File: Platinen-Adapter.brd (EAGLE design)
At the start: 26 x 100 mm, 2 parts, among them X1 MAC64L

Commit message: Layouts angepasst
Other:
- board text added: "1"
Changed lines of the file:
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@@
 <dimension x1="0" y1="-0.47" x2="0" y2="99.53" x3="-16.51" y3="49.53" textsize="1.778" layer="47"/>
 <dimension x1="0" y1="-0.47" x2="26" y2="-0.47" x3="13" y3="-12.7" textsize="1.778" layer="47"/>
-<text x="19.05" y="64.77" size="1.778" layer="25" rot="R90" align="top-center">Rev 2019/04
+<text x="18.415" y="69.85" size="2.54" layer="25" font="vector" ratio="15" rot="R90" align="top-center">Rev 2019/04
 (c) Peter Müller</text>
-<text x="19.05" y="34.29" size="1.778" layer="25" rot="R90" align="top-center">HomePi
+<text x="18.415" y="30.48" size="2.54" layer="25" font="vector" ratio="15" rot="R90" align="top-center">HomePi
 Adapter-Board</text>
+<text x="18.415" y="10.795" size="1.778" layer="25" font="vector" ratio="10" align="center">1</text>
+<text x="18.415" y="69.85" size="2.54" layer="26" font="vector" ratio="15" rot="SMR270" align="top-center">HomePi
+Adapter-Board</text>
+<text x="18.415" y="30.48" size="2.54" layer="26" font="vector" ratio="15" rot="SMR270" align="top-center">Rev 2019/04
+(c) Peter Müller</text>
 </plain>
 <attributes>
@@
 <classes>
 <class number="0" name="default" width="0" drill="0">
+</class>
+<class number="1" name="24V" width="0.8128" drill="0">
+<clearance class="1" value="0.4064"/>
 </class>
 </classes>
@@
 <elements>
 <element name="SV1" library="64-pol-verbinder" package="1X31" value="" x="15.875" y="48.26" smashed="yes" rot="R90">
-<attribute name="NAME" x="14.5288" y="91.3638" size="1.27" layer="25" ratio="10"/>
 <attribute name="VALUE" x="19.05" y="10.16" size="1.27" layer="27" rot="R90"/>
 </element>
@@
 <wire x1="5.08" y1="83.82" x2="10.16" y2="83.82" width="0.8128" layer="1"/>
 </signal>
-<signal name="+24V">
+<signal name="+24V" class="1">
 <contactref element="X1" pad="A32"/>
 <contactref element="X1" pad="C32"/>

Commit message: Layouts angepasst
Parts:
- added U$2: (no value), cryCode-Logo:30MM
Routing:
- added copper zone on layer 16, net BOT
- added copper zone on layer 1, net TOP
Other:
- board size 26 x 100 mm -> 30 x 100 mm
- board text added: "BOT"
- board text added: "Rev 2019/05 (c) Peter Müller"
- board text added: "TOP"
- board text removed: "Rev 2019/04 (c) Peter Müller"
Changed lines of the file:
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@@
 <layer number="51" name="tDocu" color="7" fill="1" visible="yes" active="yes"/>
 <layer number="52" name="bDocu" color="7" fill="1" visible="yes" active="yes"/>
+<layer number="53" name="tGND_GNDA" color="7" fill="1" visible="no" active="no"/>
+<layer number="54" name="bGND_GNDA" color="7" fill="1" visible="no" active="no"/>
+<layer number="56" name="wert" color="7" fill="1" visible="no" active="no"/>
 <layer number="90" name="Modules" color="5" fill="1" visible="no" active="no"/>
 <layer number="91" name="Nets" color="2" fill="1" visible="no" active="no"/>
@@
 <layer number="98" name="Guide" color="6" fill="1" visible="no" active="no"/>
 <layer number="99" name="SpiceOrder" color="5" fill="1" visible="no" active="no"/>
+<layer number="100" name="Muster" color="7" fill="1" visible="yes" active="yes"/>
+<layer number="101" name="Flex-Kleb" color="7" fill="1" visible="yes" active="yes"/>
+<layer number="102" name="fp2" color="7" fill="1" visible="yes" active="yes"/>
+<layer number="103" name="fp3" color="7" fill="1" visible="yes" active="yes"/>
+<layer number="104" name="fp4" color="7" fill="1" visible="yes" active="yes"/>
+<layer number="105" name="Beschreib" color="7" fill="1" visible="yes" active="yes"/>
+<layer number="106" name="BGA-Top" color="7" fill="1" visible="yes" active="yes"/>
+<layer number="107" name="BD-Top" color="7" fill="1" visible="yes" active="yes"/>
+<layer number="108" name="fp8" color="7" fill="1" visible="yes" active="yes"/>
+<layer number="109" name="fp9" color="7" fill="1" visible="yes" active="yes"/>
+<layer number="110" name="fp0" color="7" fill="1" visible="yes" active="yes"/>
+<layer number="111" name="bdokum" color="7" fill="1" visible="yes" active="yes"/>
+<layer number="116" name="Patch_BOT" color="7" fill="1" visible="yes" active="yes"/>
+<layer number="121" name="tTestdril" color="7" fill="1" visible="yes" active="yes"/>
+<layer number="122" name="bTestdril" color="7" fill="1" visible="yes" active="yes"/>
+<layer number="123" name="tTestmark" color="7" fill="1" visible="yes" active="yes"/>
+<layer number="124" name="bTestmark" color="7" fill="1" visible="yes" active="yes"/>
+<layer number="125" name="tNamesSMD" color="7" fill="1" visible="yes" active="yes"/>
+<layer number="126" name="bNamesSMD" color="7" fill="1" visible="yes" active="yes"/>
+<layer number="127" name="tValueSMD" color="7" fill="1" visible="yes" active="yes"/>
+<layer number="128" name="bValueSMD" color="7" fill="1" visible="yes" active="yes"/>
+<layer number="131" name="tAdjust" color="7" fill="1" visible="yes" active="yes"/>
+<layer number="132" name="bAdjust" color="7" fill="1" visible="yes" active="yes"/>
+<layer number="144" name="Drill_legend" color="7" fill="1" visible="no" active="yes"/>
+<layer number="151" name="tDocuSMD" color="7" fill="1" visible="yes" active="yes"/>
+<layer number="152" name="bDocuSMD" color="7" fill="1" visible="yes" active="yes"/>
+<layer number="199" name="Contour" color="7" fill="1" visible="yes" active="yes"/>
+<layer number="200" name="200bmp" color="1" fill="10" visible="yes" active="yes"/>
+<layer number="201" name="201bmp" color="7" fill="1" visible="yes" active="yes"/>
+<layer number="202" name="202bmp" color="7" fill="1" visible="yes" active="yes"/>
+<layer number="203" name="203bmp" color="7" fill="1" visible="yes" active="yes"/>
+<layer number="204" name="204bmp" color="7" fill="1" visible="yes" active="yes"/>
+<layer number="205" name="205bmp" color="7" fill="1" visible="yes" active="yes"/>
+<layer number="206" name="206bmp" color="7" fill="1" visible="yes" active="yes"/>
+<layer number="207" name="207bmp" color="7" fill="1" visible="yes" active="yes"/>
+<layer number="208" name="208bmp" color="7" fill="1" visible="yes" active="yes"/>
+<layer number="209" name="209bmp" color="7" fill="1" visible="yes" active="yes"/>
+<layer number="210" name="210bmp" color="7" fill="1" visible="yes" active="yes"/>
+<layer number="211" name="211bmp" color="7" fill="1" visible="no" active="yes"/>
+<layer number="212" name="212bmp" color="7" fill="1" visible="no" active="yes"/>
+<layer number="213" name="213bmp" color="7" fill="1" visible="no" active="yes"/>
+<layer number="214" name="214bmp" color="7" fill="1" visible="no" active="yes"/>
+<layer number="215" name="215bmp" color="7" fill="1" visible="no" active="yes"/>
+<layer number="216" name="216bmp" color="7" fill="1" visible="no" active="yes"/>
+<layer number="217" name="217bmp" color="18" fill="1" visible="no" active="no"/>
+<layer number="218" name="218bmp" color="19" fill="1" visible="no" active="no"/>
+<layer number="219" name="219bmp" color="20" fill="1" visible="no" active="no"/>
+<layer number="220" name="220bmp" color="21" fill="1" visible="no" active="no"/>
+<layer number="221" name="221bmp" color="22" fill="1" visible="no" active="no"/>
+<layer number="222" name="222bmp" color="23" fill="1" visible="no" active="no"/>
+<layer number="223" name="223bmp" color="24" fill="1" visible="no" active="no"/>
+<layer number="224" name="224bmp" color="25" fill="1" visible="no" active="no"/>
 <layer number="250" name="Descript" color="3" fill="1" visible="no" active="no"/>
 <layer number="251" name="SMDround" color="12" fill="11" visible="no" active="no"/>
+<layer number="254" name="OrgLBR" color="7" fill="1" visible="yes" active="yes"/>
 </layers>
 <board>
 <plain>
-<wire x1="0" y1="-0.47" x2="26" y2="-0.47" width="0.2" layer="20"/>
-<wire x1="26" y1="-0.47" x2="26" y2="99.53" width="0.2" layer="20"/>
-<wire x1="26" y1="99.53" x2="0" y2="99.53" width="0.2" layer="20"/>
+<wire x1="0" y1="-0.47" x2="30" y2="-0.47" width="0.2" layer="20"/>
+<wire x1="30" y1="-0.47" x2="30" y2="99.53" width="0.2" layer="20"/>
+<wire x1="30" y1="99.53" x2="0" y2="99.53" width="0.2" layer="20"/>
 <wire x1="0" y1="99.53" x2="0" y2="-0.47" width="0.2" layer="20"/>
-<dimension x1="15.875" y1="48.26" x2="26" y2="48.26" x3="20.9375" y3="-6.35" textsize="1.778" layer="47"/>
-<dimension x1="0" y1="-0.47" x2="0" y2="99.53" x3="-16.51" y3="49.53" textsize="1.778" layer="47"/>
-<dimension x1="0" y1="-0.47" x2="26" y2="-0.47" x3="13" y3="-12.7" textsize="1.778" layer="47"/>
-<text x="18.415" y="69.85" size="2.54" layer="25" font="vector" ratio="15" rot="R90" align="top-center">Rev 2019/04
+<dimension x1="15.875" y1="48.26" x2="30" y2="48.26" x3="22.9375" y3="-6.35" textsize="1.778" layer="47" visible="yes"/>
+<dimension x1="0" y1="-0.47" x2="0" y2="99.53" x3="-16.51" y3="49.53" textsize="1.778" layer="47" visible="yes"/>
+<dimension x1="0" y1="-0.47" x2="30" y2="-0.47" x3="15" y3="-12.7" textsize="1.778" layer="47" visible="yes"/>
+<text x="19.685" y="69.85" size="2.54" layer="25" font="vector" ratio="15" rot="R90" align="top-center">Rev 2019/05
 (c) Peter Müller</text>
-<text x="18.415" y="30.48" size="2.54" layer="25" font="vector" ratio="15" rot="R90" align="top-center">HomePi
+<text x="19.685" y="30.48" size="2.54" layer="25" font="vector" ratio="15" rot="R90" align="top-center">HomePi
 Adapter-Board</text>
 <text x="18.415" y="10.795" size="1.778" layer="25" font="vector" ratio="10" align="center">1</text>
-<text x="18.415" y="69.85" size="2.54" layer="26" font="vector" ratio="15" rot="SMR270" align="top-center">HomePi
-Adapter-Board</text>
-<text x="18.415" y="30.48" size="2.54" layer="26" font="vector" ratio="15" rot="SMR270" align="top-center">Rev 2019/04
-(c) Peter Müller</text>
+<text x="10.16" y="2.8575" size="1.27" layer="42" font="vector" ratio="15" rot="MR0">BOT</text>
+<text x="10.16" y="2.8575" size="1.27" layer="41" font="vector" ratio="15" align="bottom-right">TOP</text>
 </plain>
 <attributes>
@@
 <attribute name="VALUE" x="-5.08" y="60.9854" size="1.27" layer="27" ratio="10" rot="R270"/>
 </element>
+<element name="U$2" library="cryCode-Logo" package="30MM" value="" x="26.67" y="64.77" rot="MR270"/>
 </elements>
 <signals>
@@
 <signal name="GND">
 <polygon width="0.254" layer="16" isolate="0.254">
-<vertex x="1.905" y="90.17"/>
-<vertex x="18.415" y="90.17"/>
-<vertex x="18.415" y="8.89"/>
-<vertex x="1.905" y="8.89"/>
+<vertex x="1.905" y="91.44"/>
+<vertex x="18.415" y="91.44"/>
+<vertex x="18.415" y="7.62"/>
+<vertex x="1.905" y="7.62"/>
 </polygon>
 <contactref element="SV1" pad="29"/>
@@
 <contactref element="X1" pad="A26"/>
 </signal>
+<signal name="TOP">
+<polygon width="0.254" layer="1" orphans="yes">
+<vertex x="6.35" y="4.445"/>
+<vertex x="10.795" y="4.445"/>
+<vertex x="10.795" y="2.54"/>
+<vertex x="6.35" y="2.54"/>
+</polygon>
+</signal>
+<signal name="BOT">
+<polygon width="0.254" layer="16" orphans="yes">
+<vertex x="6.35" y="4.445"/>
+<vertex x="10.795" y="4.445"/>
+<vertex x="10.795" y="2.54"/>
+<vertex x="6.35" y="2.54"/>
+</polygon>
+</signal>
 </signals>

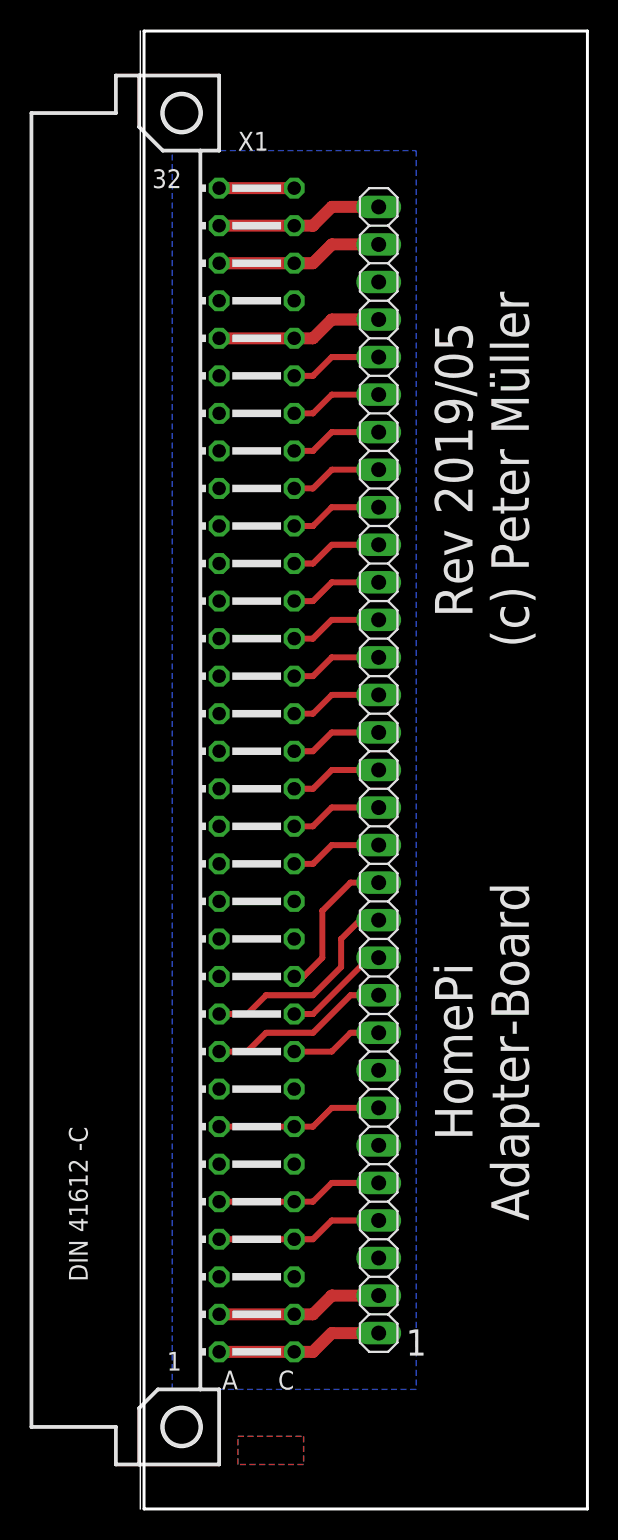
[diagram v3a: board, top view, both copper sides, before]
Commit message: Leiterplatten verkleinert zur Kostenerspranis
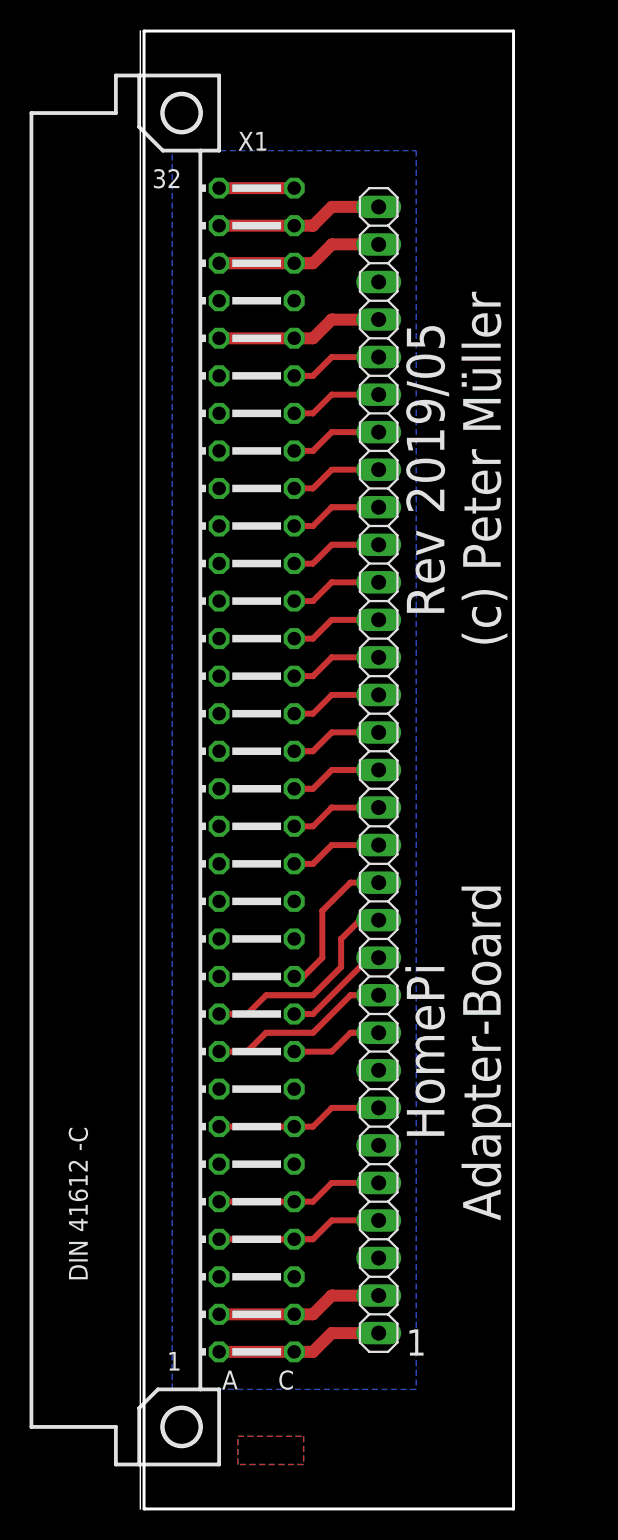
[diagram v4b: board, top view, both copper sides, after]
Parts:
- moved U$2 2.54 mm to (24.1, 64.8)
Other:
- board size 30 x 100 mm -> 25 x 100 mm
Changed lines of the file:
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@@
 <board>
 <plain>
-<wire x1="0" y1="-0.47" x2="30" y2="-0.47" width="0.2" layer="20"/>
-<wire x1="30" y1="-0.47" x2="30" y2="99.53" width="0.2" layer="20"/>
-<wire x1="30" y1="99.53" x2="0" y2="99.53" width="0.2" layer="20"/>
+<wire x1="0" y1="-0.47" x2="25" y2="-0.47" width="0.2" layer="20"/>
+<wire x1="25" y1="-0.47" x2="25" y2="99.53" width="0.2" layer="20"/>
+<wire x1="25" y1="99.53" x2="0" y2="99.53" width="0.2" layer="20"/>
 <wire x1="0" y1="99.53" x2="0" y2="-0.47" width="0.2" layer="20"/>
-<dimension x1="15.875" y1="48.26" x2="30" y2="48.26" x3="22.9375" y3="-6.35" textsize="1.778" layer="47" visible="yes"/>
+<dimension x1="15.875" y1="48.26" x2="25" y2="48.26" x3="20.4375" y3="-6.35" textsize="1.778" layer="47" visible="yes"/>
 <dimension x1="0" y1="-0.47" x2="0" y2="99.53" x3="-16.51" y3="49.53" textsize="1.778" layer="47" visible="yes"/>
-<dimension x1="0" y1="-0.47" x2="30" y2="-0.47" x3="15" y3="-12.7" textsize="1.778" layer="47" visible="yes"/>
-<text x="19.685" y="69.85" size="2.54" layer="25" font="vector" ratio="15" rot="R90" align="top-center">Rev 2019/05
+<dimension x1="0" y1="-0.47" x2="25" y2="-0.47" x3="12.5" y3="-12.7" textsize="1.778" layer="47" visible="yes"/>
+<text x="17.78" y="69.85" size="2.54" layer="25" font="vector" ratio="15" rot="R90" align="top-center">Rev 2019/05
 (c) Peter Müller</text>
-<text x="19.685" y="30.48" size="2.54" layer="25" font="vector" ratio="15" rot="R90" align="top-center">HomePi
+<text x="17.78" y="30.48" size="2.54" layer="25" font="vector" ratio="15" rot="R90" align="top-center">HomePi
 Adapter-Board</text>
 <text x="18.415" y="10.795" size="1.778" layer="25" font="vector" ratio="10" align="center">1</text>
@@
 <attribute name="VALUE" x="-5.08" y="60.9854" size="1.27" layer="27" ratio="10" rot="R270"/>
 </element>
-<element name="U$2" library="cryCode-Logo" package="30MM" value="" x="26.67" y="64.77" rot="MR270"/>
+<element name="U$2" library="cryCode-Logo" package="30MM" value="" x="24.13" y="64.77" rot="MR270"/>
 </elements>
 <signals>
